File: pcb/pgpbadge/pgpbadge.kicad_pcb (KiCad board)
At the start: 4 copper layers, 28.3 x 52.6 mm, 60 parts, among them J1 UJ31-CH-3-SMT-TR_official, M1 SSD1306, Q1 Q_DNPN, U1 LM3658, U2 BQ27542DRZR-G1, U3 TPS63030DSKR, U4 CP2102N-A01-GQFN24, U5 ESP32-WROOM-32

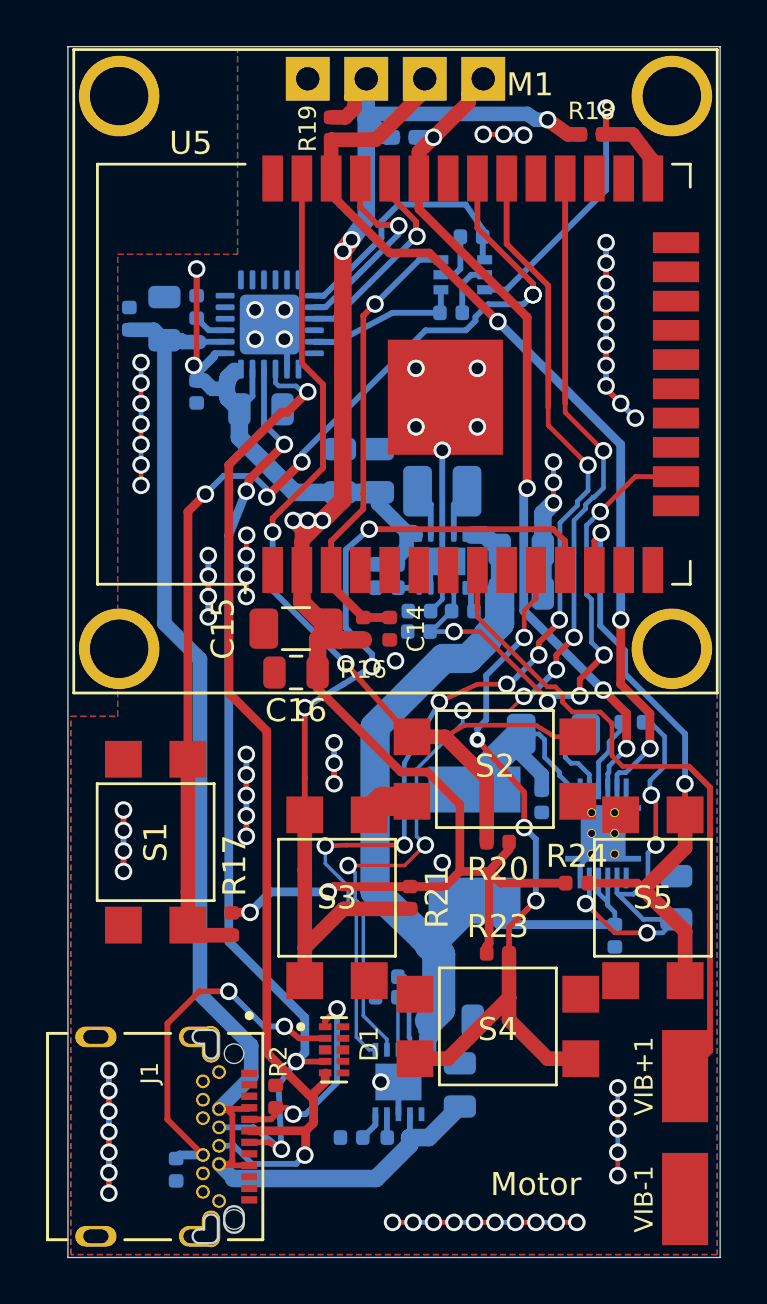
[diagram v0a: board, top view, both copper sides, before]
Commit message: Fixed DRCs except USB C
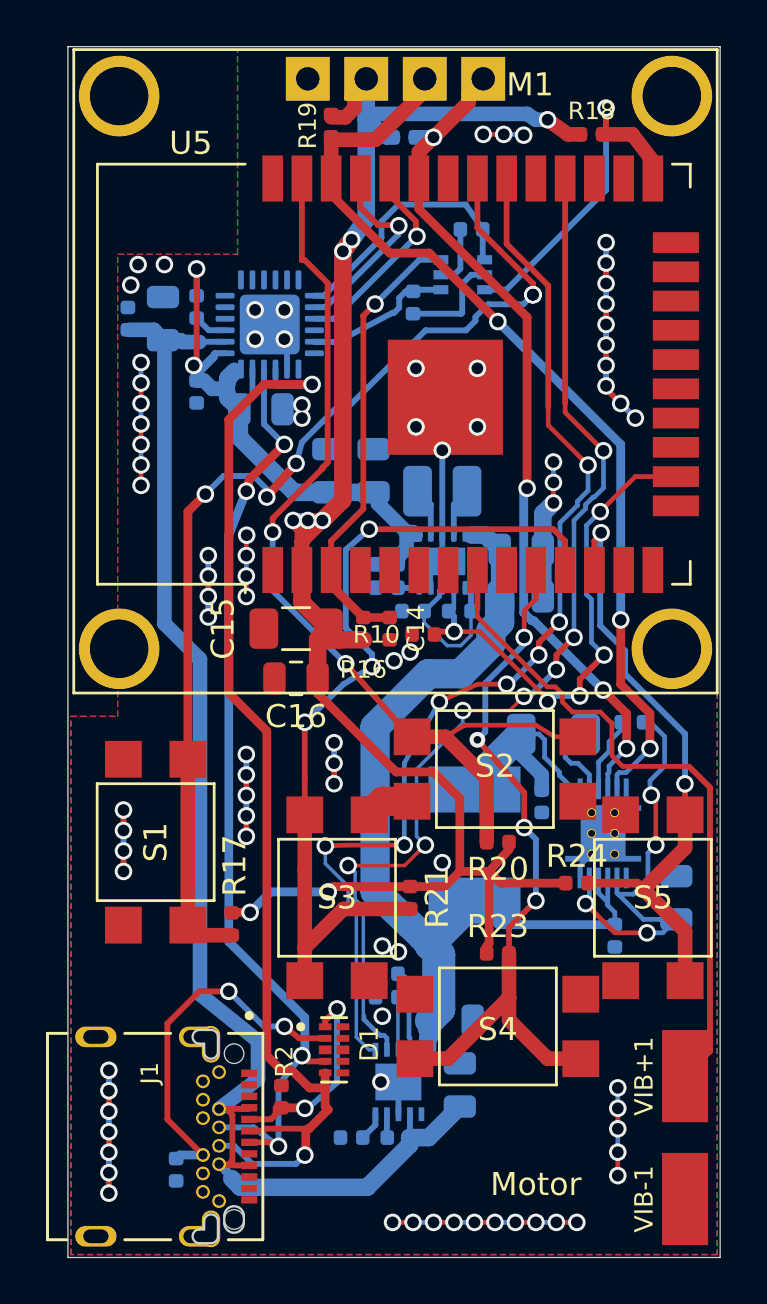
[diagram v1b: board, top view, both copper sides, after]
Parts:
- R10: moved to F.Cu
- moved R14 1.71 mm to (217.9, 73.2), turned to 270 degrees
- moved C9 0.51 mm to (214.2, 80.5)
- moved R15 0.32 mm to (220.5, 70.0)
- moved C7 0.28 mm to (217.9, 86.6)
- moved R2 0.25 mm to (212.2, 107.7)
- moved C16 0.25 mm to (212.9, 89.5)
- moved R10 0.23 mm to (218.4, 87.6)
- moved C8 0.19 mm to (216.2, 80.5)
- moved R19 0.13 mm to (214.4, 65.5)
- moved R6 0.13 mm to (216.8, 102.4)
- moved R9 0.13 mm to (220.0, 86.6)
- moved C6 0.13 mm to (222.6, 86.0)
- moved C10 0.06 mm to (207.1, 73.9)
- moved C11 0.06 mm to (205.5, 73.9)
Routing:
- net Net-(C7-Pad1): track 2.33 -> 6.65 mm
- net Net-(Q1-Pad2): track 2.39 -> 4.55 mm
- net /system.sch/USBP: track 47.2 -> 48.7 mm
- net /Power/USB5v: track 60.6 -> 61.6 mm
- net GND: track 81.1 -> 81.9 mm, vias 77 -> 86
- net /Power/BULK: track 44.2 -> 45.0 mm
- net /system.sch/USBN: track 42.6 -> 42.0 mm
- net Net-(D1-Pad1): track 9.07 -> 8.56 mm
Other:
- rule trace_min: 0.000152 -> 0.1524
- rule via_min_size: 0.000508 -> 0.508

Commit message: DRC's clean, silscreen updated, 1ks changed to 5.6k
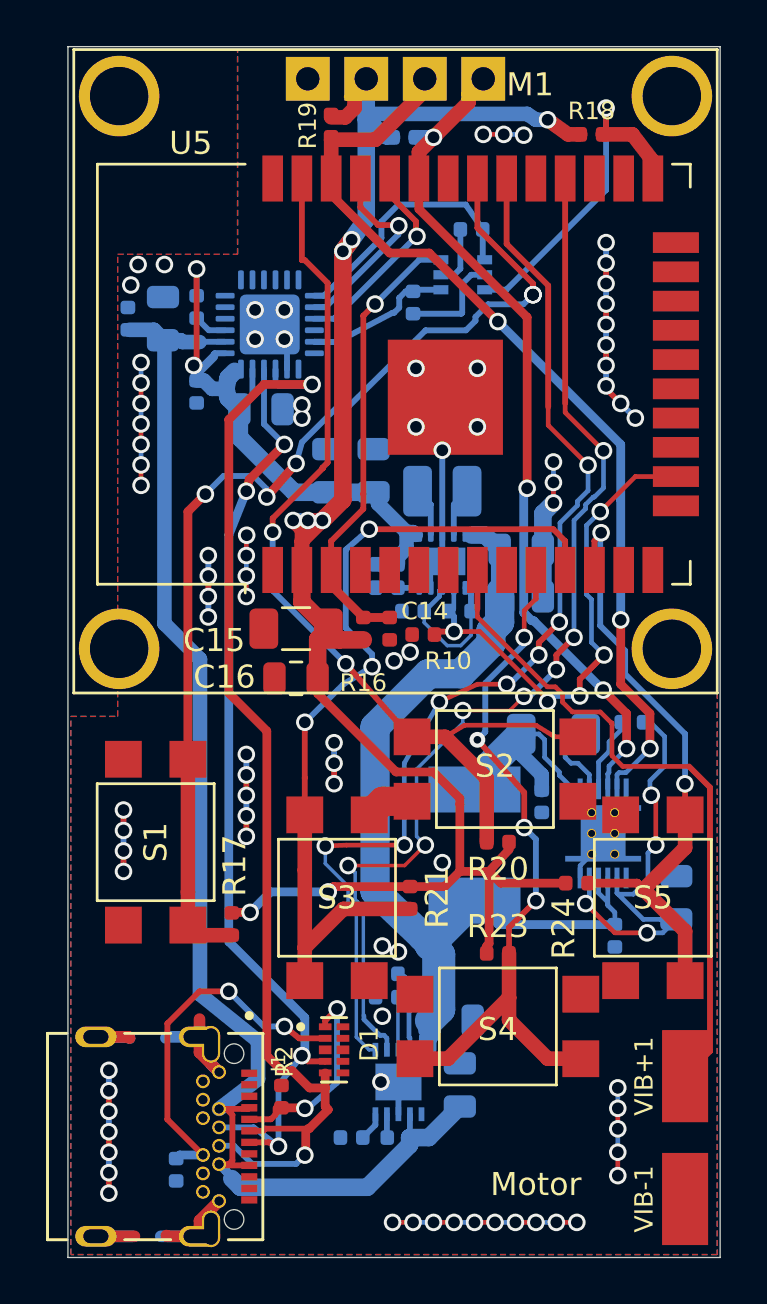
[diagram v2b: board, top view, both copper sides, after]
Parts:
- J1: footprint CUI_UJ31-CH-3-SMT-TR -> pgpbadge:CUI_UJ31-CH-3-SMT-TR
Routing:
- net GND: track 81.9 -> 98.7 mm
